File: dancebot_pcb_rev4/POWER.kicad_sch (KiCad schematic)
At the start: 21 parts, among them IC201 TPS63000IDRCRQ1, J201 1769

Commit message: schematic ready for review!
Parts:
- added TP2: USBC_ST, TestPoint:TestPoint_Pad_1.0x1.0mm, symbol Connector:TestPoint
- added TP3: BAT_ST, TestPoint:TestPoint_Pad_1.0x1.0mm, symbol Connector:TestPoint
- J201: value 1769 -> BatteryJ ST Connector
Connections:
- net BAT_ST: now also TP3.1
- net USBC_ST: now also TP2.1
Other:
- note added: "Hierarchical Labels"
- moved on the sheet: C201, C202, C203, C204, C205, C206, C207, D201, D202, D203, IC201, J201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

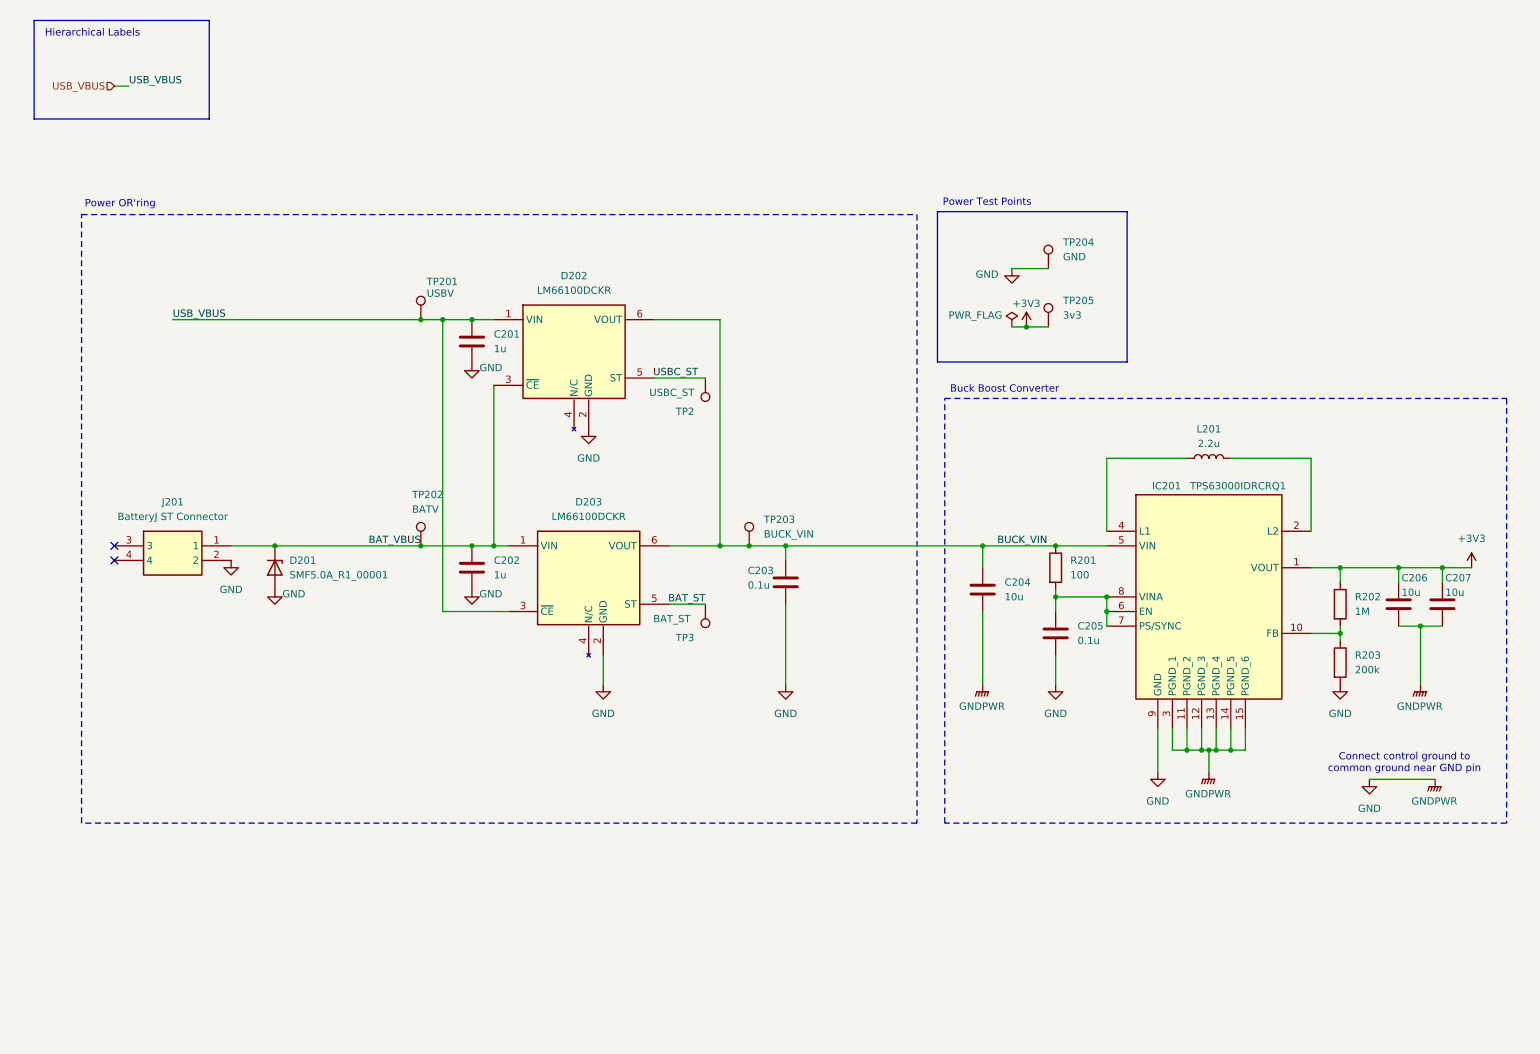
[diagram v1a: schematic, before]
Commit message: now using ESP32-S3-WROOM-1, changed power delivery system
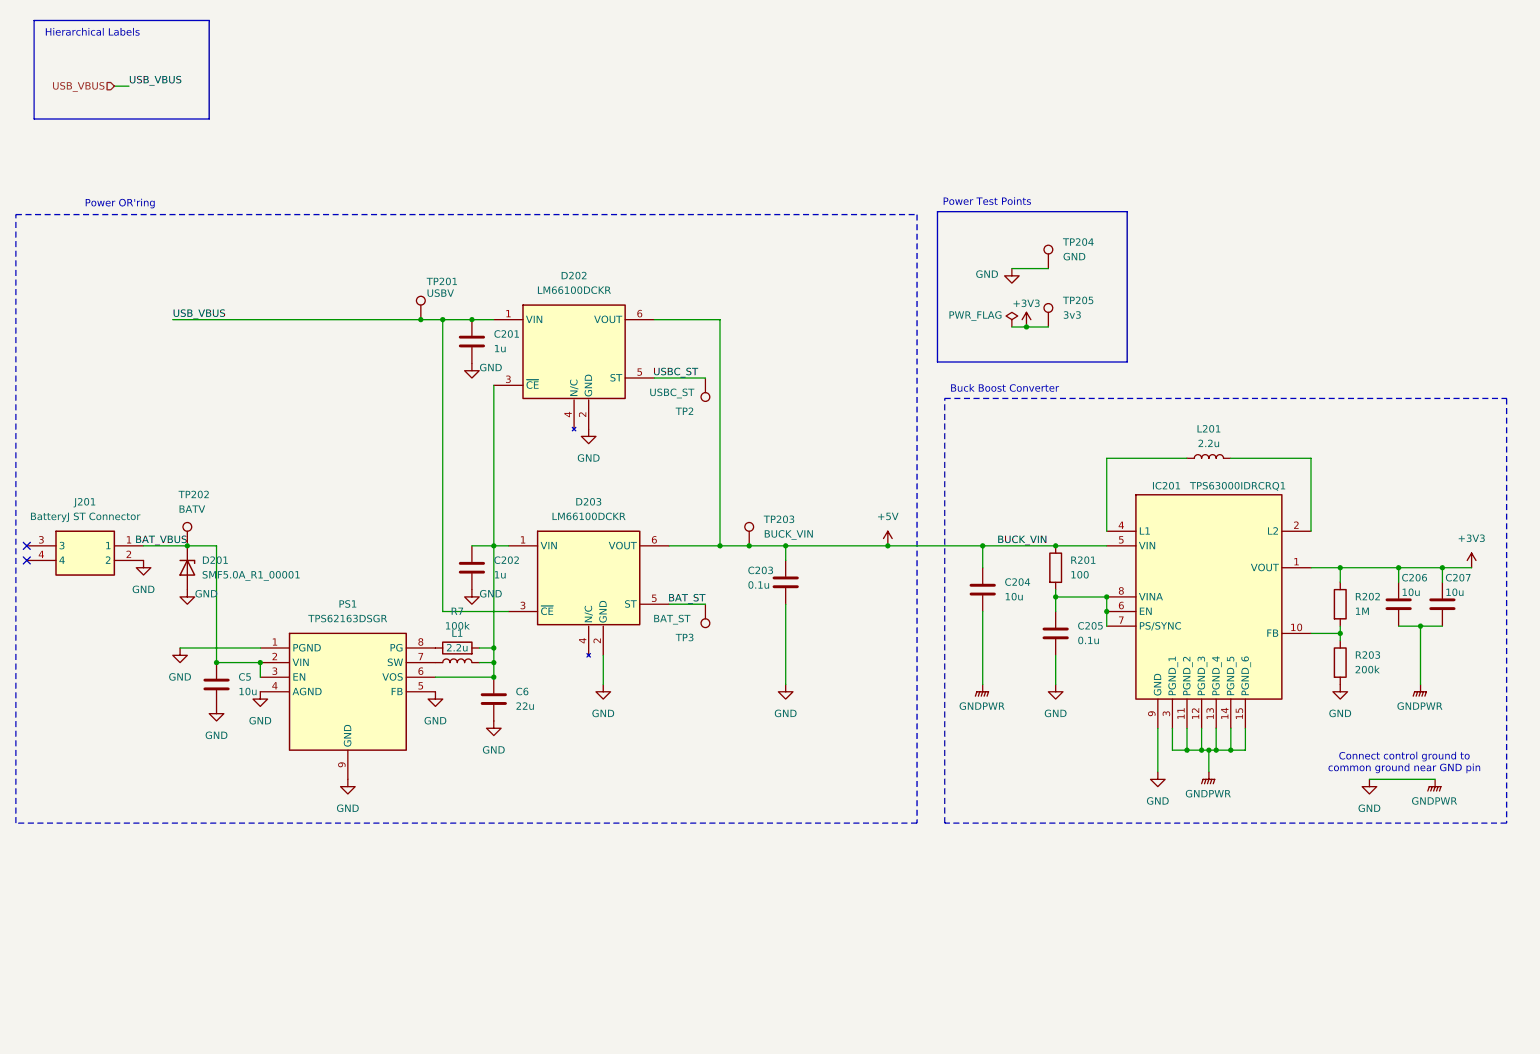
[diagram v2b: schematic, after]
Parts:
- added C5: 10u, SamacSys_Parts:CAPC1608X80N, symbol Device:C
- added C6: 22u, SamacSys_Parts:CAPC2012X145N, symbol Device:C
- added L1: 2.2u, SamacSys_Parts:NRS3015T2R2MNGHV, symbol Device:L
- added PS1: TPS62163DSGR, SamacSys_Parts:SON50P200X200X80-9N, symbol SamacSys_Parts:TPS62163DSGR
- added R7: 100k, SamacSys_Parts:RESC2012X50N, symbol Device:R
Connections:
- net BAT_VBUS: now also C5.1, PS1.2 (VIN), PS1.3 (EN); no longer C202.1, D202.3 (~{CE}), D203.1 (VIN)
- net GND: now also C5.2, C6.2, PS1.1 (PGND), PS1.4 (AGND), PS1.5 (FB), PS1.9 (GND)
- net BUCK_VIN renamed +5V
- new net: L1.1, PS1.7 (SW)
- new net: C202.1, C6.1, D202.3 (~{CE}), D203.1 (VIN), L1.2, PS1.6 (VOS), R7.2
- new net: PS1.8 (PG), R7.1
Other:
- moved on the sheet: D201, J201, TP202

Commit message: fixed some issues with labels
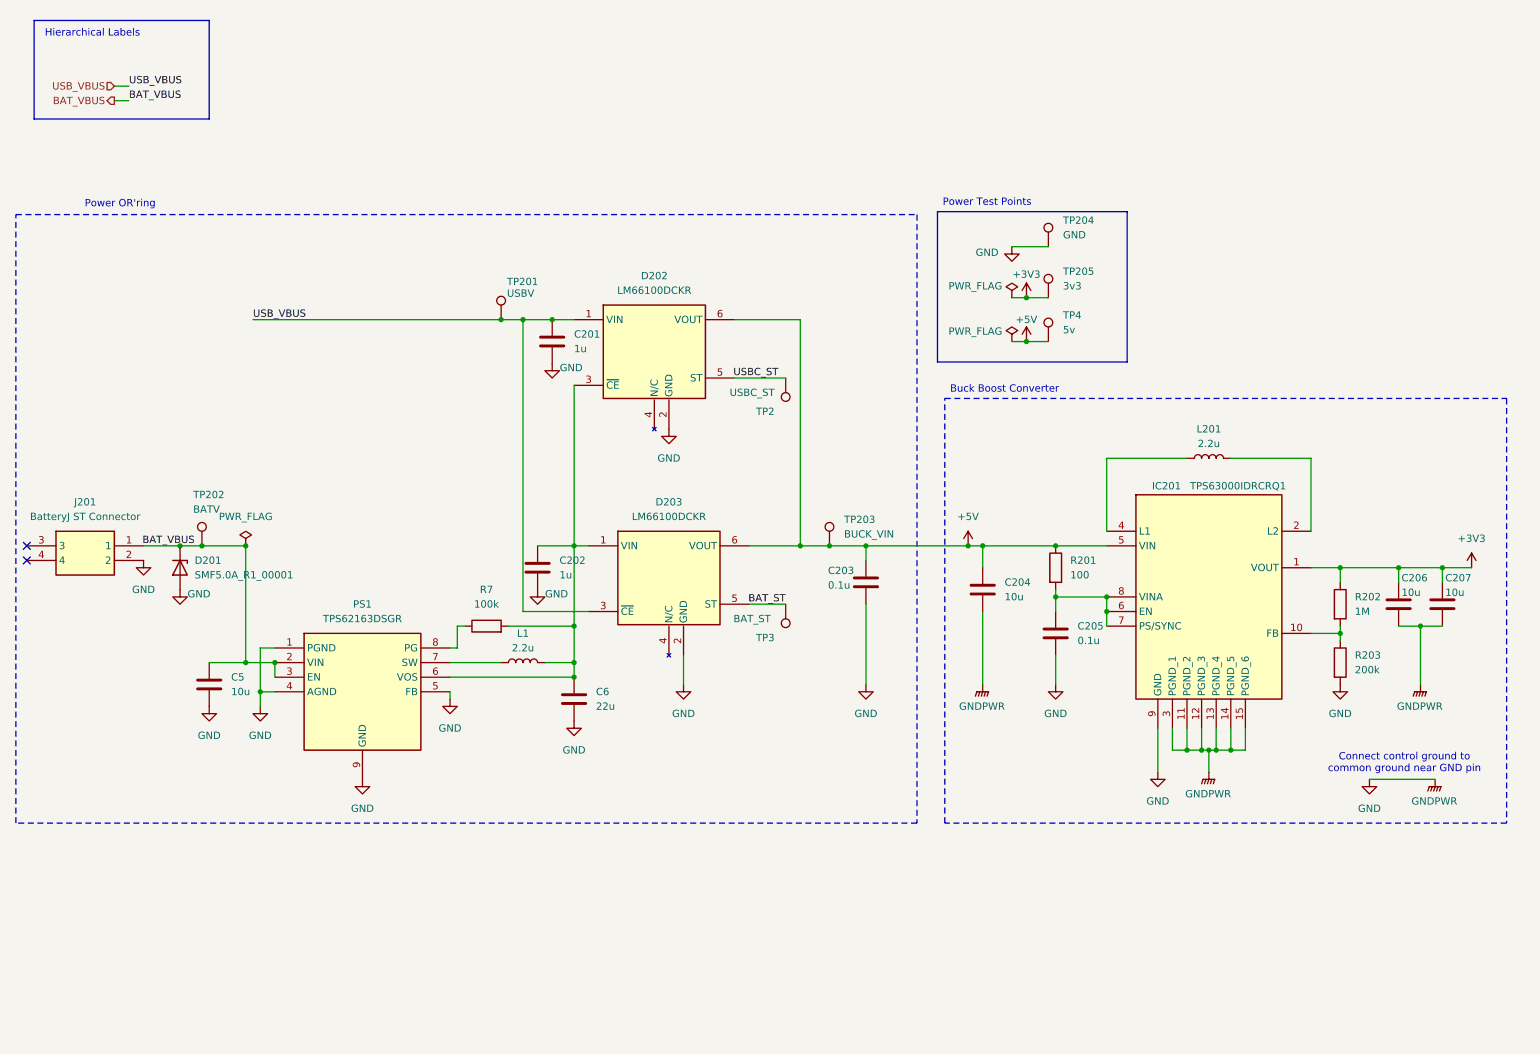
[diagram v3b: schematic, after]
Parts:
- added TP4: 5v, symbol Connector:TestPoint
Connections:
- net +5V: now also TP4.1
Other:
- moved on the sheet: C201, C202, C203, C5, C6, D201, D202, D203, L1, PS1, R7, TP2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

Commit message: first routing iteration
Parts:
- removed TP203: BUCK_VIN, TestPoint:TestPoint_Pad_1.0x1.0mm, symbol Connector:TestPoint
- TP4: footprint (none) -> TestPoint:TestPoint_Pad_1.0x1.0mm
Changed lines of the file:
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@@
 	)
 	(junction
-		(at 154.94 106.68)
-		(diameter 0)
-		(color 0 0 0 0)
-	)
-	(junction
 		(at 219.71 142.24)
 		(diameter 0)
@@
 	(wire
 		(pts
-			(xy 149.86 106.68) (xy 154.94 106.68)
-		)
-		(stroke
-			(width 0)
-			(type default)
-		)
-	)
-	(wire
-		(pts
 			(xy 55.88 132.08) (xy 58.42 132.08)
 		)
@@
 	(wire
 		(pts
-			(xy 154.94 106.68) (xy 161.29 106.68)
+			(xy 149.86 106.68) (xy 161.29 106.68)
 		)
 		(stroke
@@
 			)
 		)
-		(property "Footprint" ""
+		(property "Footprint" "TestPoint:TestPoint_Pad_1.0x1.0mm"
 			(at 198.12 71.12 0)
 			(effects
@@
 					(unit 1)
 				)
-			)
-		)
-	)
-	(symbol
-		(lib_id "Connector:TestPoint")
-		(at 154.94 106.68 0)
-		(unit 1)
-		(exclude_from_sim no)
-		(in_bom yes)
-		(on_board yes)
-		(dnp no)
-		(fields_autoplaced yes)
-		(property "Reference" "TP203"
-			(at 157.48 102.1079 0)
-			(effects
-				(font
-					(size 1.27 1.27)
-				)
-				(justify left)
-			)
-		)
-		(property "Value" "BUCK_VIN"
-			(at 157.48 104.6479 0)
-			(effects
-				(font
-					(size 1.27 1.27)
-				)
-				(justify left)
-			)
-		)
-		(property "Footprint" "TestPoint:TestPoint_Pad_1.0x1.0mm"
-			(at 160.02 106.68 0)
-			(effects
-				(font
-					(size 1.27 1.27)
-				)
-				(hide yes)
-			)
-		)
-		(property "Datasheet" "~"
-			(at 160.02 106.68 0)
-			(effects
-				(font
-					(size 1.27 1.27)
-				)
-				(hide yes)
-			)
-		)
-		(property "Description" "test point"
-			(at 154.94 106.68 0)
-			(effects
-				(font
-					(size 1.27 1.27)
-				)
-				(hide yes)
-			)
-		)
-		(property "MAXIMUM_PACKAGE_HEIGHT" ""
-			(at 154.94 106.68 0)
-			(effects
-				(font
-					(size 1.27 1.27)
-				)
-				(hide yes)
-			)
-		)
-		(pin "1"
-		)
-		(instances
-			(project "Dancebot_PCB"
-				(path "/21324b60-e5e7-4de6-a38d-f4cdf81a1b2c/9bb1d94d-135a-4bfe-a8c4-60fef77f5043"
-					(reference "TP203")
-					(unit 1)
-				)
